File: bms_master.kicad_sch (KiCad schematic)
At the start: 88 parts, among them J1 Conn_01x02, J2 Conn_01x02, J3 Conn_01x02, J4 Conn_01x04, J5 Conn_01x04, J6 Conn_01x06, Q1 PMV15ENE, Q2 PMV74EPE, Q3 PMV74EPE, SW1 SW_Push, U1 TPS7B88, U2 MCP1700x-330xxMB, U3 STM32F103C8Tx, U4 SN65HVD1050D, U5 M24C64-R, U6 MAX6126, U7 MAX11163, U8 741G3157, U9 TPS25961, Y1 8M

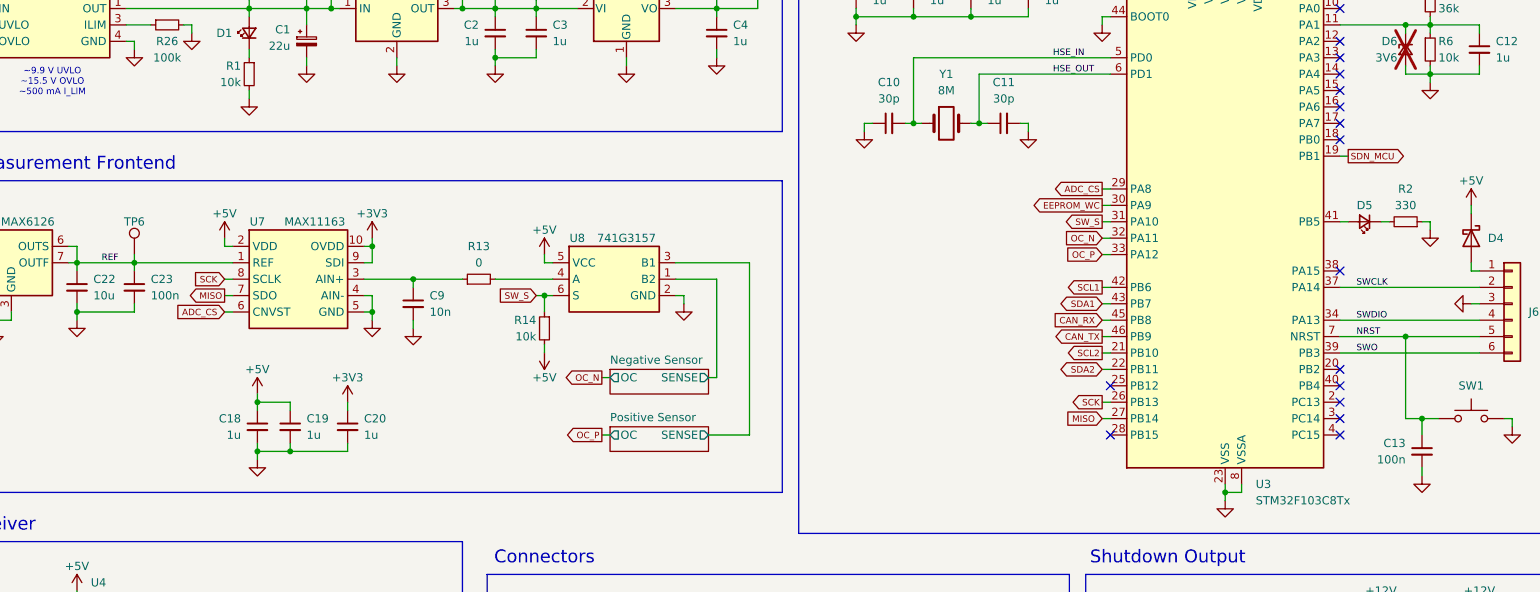
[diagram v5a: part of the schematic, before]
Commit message: *: Connect the reference to an STM ADC pin
Also change the EEPROM_WC pin.
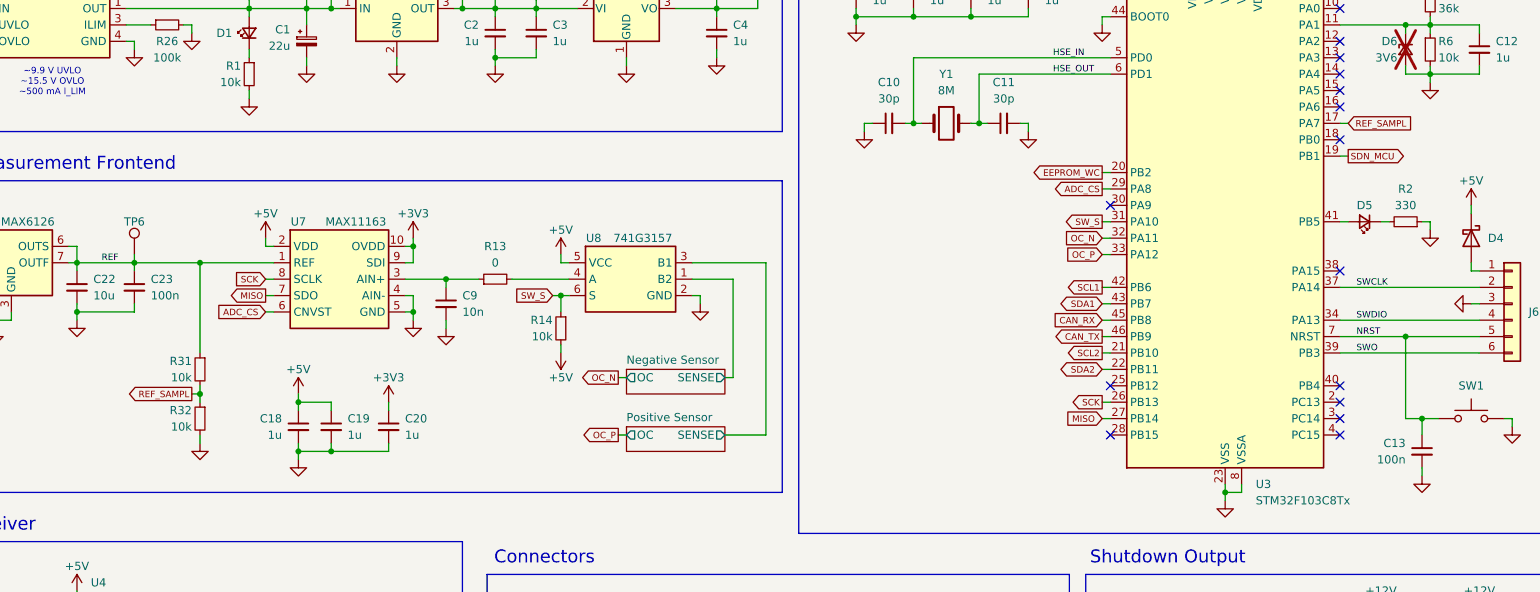
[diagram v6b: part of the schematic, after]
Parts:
- added R31, R32: 10k, Resistor_SMD:R_0603_1608Metric, symbol Device:R_Small
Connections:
- net EEPROM_WC: now also U3.20 (PB2); no longer U3.30 (PA9)
- net GND: now also R32.2
- net REF: now also R31.1
- net REF_SAMPL: now reaches U3.17 (PA7)
- net REF_SAMPL: now also R31.2, R32.1
- no-connect marks 17 -> 16
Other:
- moved on the sheet: C18, C19, C20, C9, R13, R14, U7, U8
